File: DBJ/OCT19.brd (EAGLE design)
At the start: 100 x 80 mm, 30 parts, among them IC1 ATMEGA168TQFP-08, IC2 TB6612FNG, IC3 7805DT, J1 5.5x2.1mm Barrel, Y2 16MHZ

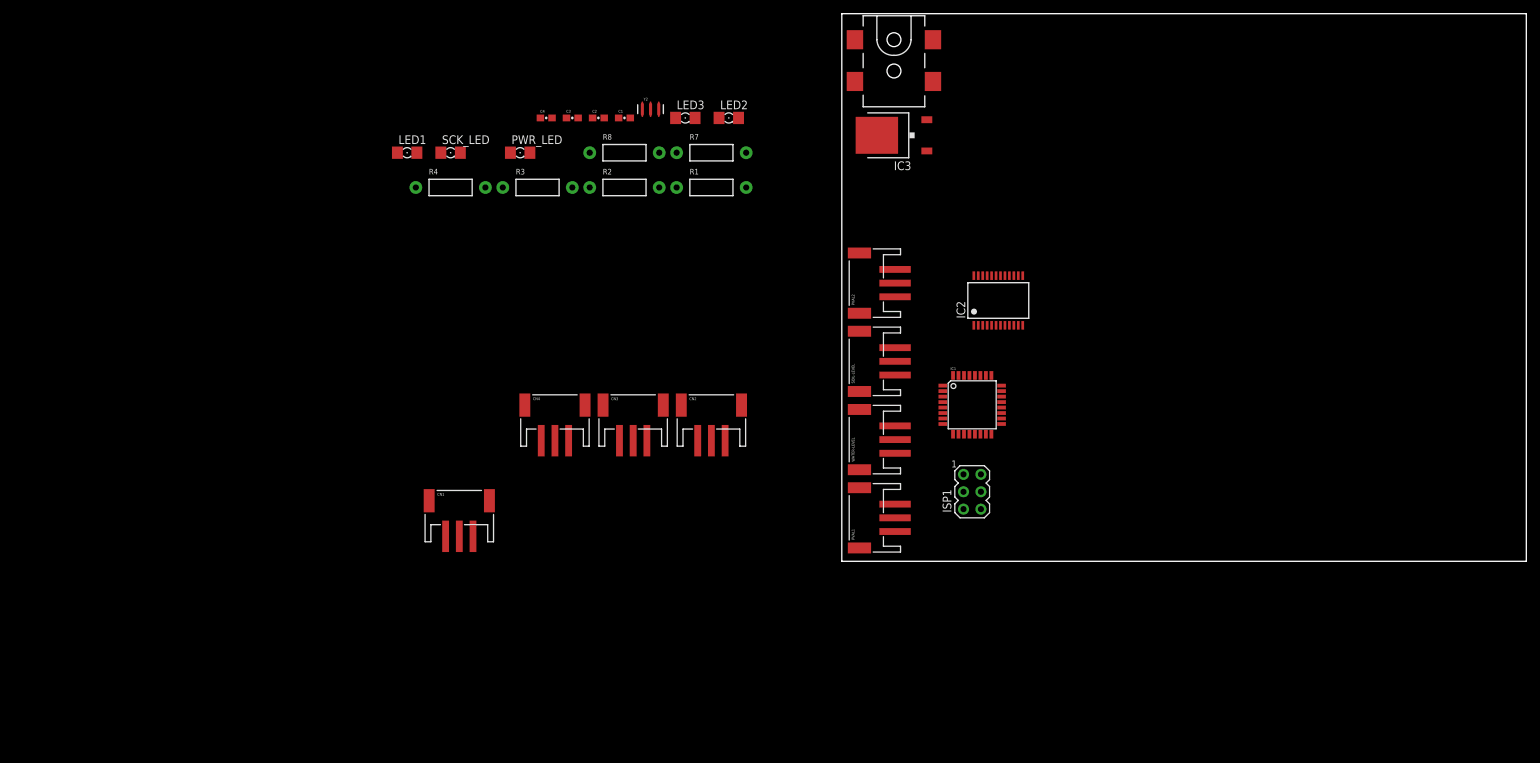
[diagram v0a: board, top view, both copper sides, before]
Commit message: sunday changes
added a push button to pc6/reset for human-interaction with the reset
line
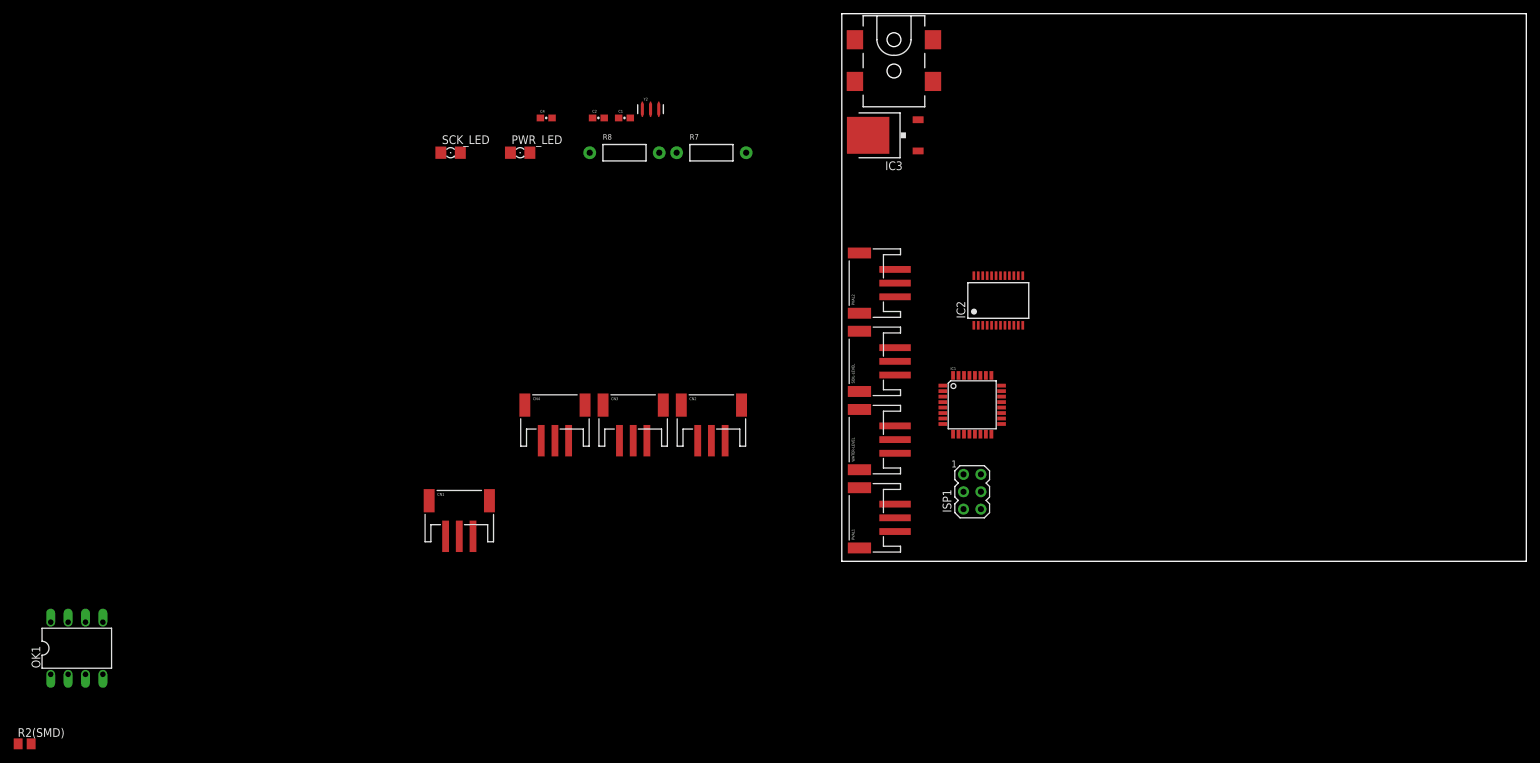
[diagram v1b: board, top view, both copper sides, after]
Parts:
- removed C3: 0.1uF, SparkFun-Capacitors:0603-CAP
- removed LED1, LED2, LED3: (no value), eagle-ltspice:LED_1206
- removed R1, R2, R3, R4: (no value), SparkFun-Resistors:AXIAL-0.4
- added OK1: PC827, optocoupler:DIL08
- added R2(SMD): (no value), adafruit:M0805
- moved IC3 1.27 mm to (6.35, 62.2)
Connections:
- net +5V: now also R2(SMD).2; no longer R1.P$2
- net GND: now also C4.1
- net N$1: now also R2(SMD).1; no longer R1.P$1
